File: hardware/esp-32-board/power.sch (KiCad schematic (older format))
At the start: 12 parts, among them J6 Barrel_Jack_MountingPin, SW3 SW_DPDT_x2, U4 NCP1117ST50T3G, U5 NCP1117-3.3

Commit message: Fix ERC errors in schematic
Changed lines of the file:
@@
 Wire Wire Line
 	5750 3300 5850 3300
-Text HLabel 5750 3300 0    50   UnSpc ~ 0
-Internal_3V3
 Text HLabel 6350 3400 2    50   UnSpc ~ 0
 +3.3V
@@
 Wire Wire Line
 	3400 3250 3950 3250
-Text HLabel 3950 3250 2    50   UnSpc ~ 0
-Internal_3V3
 Connection ~ 1950 3250
 Wire Wire Line
@@
 	2400 1550 2800 1550
 NoConn ~ 5850 3500
+Text Label 3950 3250 0    50   ~ 0
+Internal_3V3
+Text Label 5750 3300 2    50   ~ 0
+Internal_3V3
 $EndSCHEMATC

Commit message: Expose 5V instead of VIN on main connector
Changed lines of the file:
@@
 	1850 1550 2100 1550
 Wire Wire Line
-	2400 1550 2800 1550
+	2400 1550 2650 1550
 NoConn ~ 5850 3500
 Text Label 3950 3250 0    50   ~ 0
@@
 Text Label 5750 3300 2    50   ~ 0
 Internal_3V3
+$Comp
+L power:PWR_FLAG #FLG0101
+U 1 1 5FFE3888
+P 2650 1500
+F 0 "#FLG0101" H 2650 1575 50  0001 C CNN
+F 1 "PWR_FLAG" H 2650 1700 50  0000 C CNN
+F 2 "" H 2650 1500 50  0001 C CNN
+F 3 "~" H 2650 1500 50  0001 C CNN
+	1    2650 1500
+	1    0    0    -1
+$EndComp
+Wire Wire Line
+	2650 1550 2650 1500
+Connection ~ 2650 1550
+Wire Wire Line
+	2650 1550 2800 1550
 $EndSCHEMATC

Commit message: Replace power switch with jumper, add RX/TX leds
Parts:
- J7: renamed from SW3; value SW_DPDT_x2 -> Conn_01x02; footprint Button_Switch_SMD:Nidec_CL-SB-22B-0X -> Connector_PinHeader_2.54mm:PinHeader_1x02_P2.54mm_Vertical; symbol Switch:SW_DPDT_x2 -> Connector_Generic:Conn_01x02; Vendor tme.eu -> (none); VendorLink https://www.tme.eu/pl/details/cl-sb-22b-01/przelaczniki-suw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 -> (none)
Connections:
- no-connect marks 1 -> 0
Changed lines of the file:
@@
 VIN
 Wire Wire Line
-	6250 3400 6350 3400
+	5850 3500 5750 3500
 Wire Wire Line
-	5750 3300 5850 3300
-Text HLabel 6350 3400 2    50   UnSpc ~ 0
+	5750 3400 5850 3400
+Text HLabel 5750 3500 0    50   UnSpc ~ 0
 +3.3V
 $Comp
-L Switch:SW_DPDT_x2 SW3
+L Connector_Generic:Conn_01x02 J7
 U 1 1 5FE84590
 P 6050 3400
-F 0 "SW3" H 6050 3650 50  0000 C CNN
-F 1 "SW_DPDT_x2" H 6050 3550 50  0000 C CNN
-F 2 "Button_Switch_SMD:Nidec_CL-SB-22B-0X" H 6050 3050 50  0001 C CNN
-F 3 "https://www.tme.eu/Document/3439bdb81b005bcee4b59ba949df073a/seriaCL-SB.pdf" H 6050 3400 50  0001 C CNN
-F 4 "tme.eu" H 6050 3400 50  0001 C CNN "Vendor"
-F 5 "https://www.tme.eu/pl/details/cl-sb-22b-01/przelaczniki-suwakowe/nidec-copal-electronics/" H 6050 3400 50  0001 C CNN "VendorLink"
+F 0 "J7" H 6050 3650 50  0000 C CNN
+F 1 "Conn_01x02" H 6050 3550 50  0000 C CNN
+F 2 "Connector_PinHeader_2.54mm:PinHeader_1x02_P2.54mm_Vertical" H 6050 3050 50  0001 C CNN
+F 3 "~" H 6050 3400 50  0001 C CNN
+F 4 "" H 6050 3400 50  0001 C CNN "Vendor"
+F 5 "" H 6050 3400 50  0001 C CNN "VendorLink"
 	1    6050 3400
-	-1   0    0    -1
+	1    0    0    -1
 $EndComp
 Connection ~ 3400 3250
@@
 Text Notes 5200 2850 0    100  ~ 20
 Power switch for ESP-32
-Text Notes 5250 3950 0    50   ~ 0
+Text Notes 5250 4350 0    50   ~ 0
 Allows to disconnect ESP-32's 3.3V from regulators.\nUseful when board is powered externally by 3.3V port, preventing\ncurrent from "leaking" in unused USB and power circuit.
 $Comp
@@
 Wire Wire Line
 	2400 1550 2650 1550
-NoConn ~ 5850 3500
 Text Label 3950 3250 0    50   ~ 0
 Internal_3V3
-Text Label 5750 3300 2    50   ~ 0
+Text Label 5750 3400 2    50   ~ 0
 Internal_3V3
 $Comp

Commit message: Move LEDs
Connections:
- net +5V: now also D3.2 (A); no longer R4.1
- net GND: now also R4.2; no longer D3.1 (K)
- new net: D3.1 (K), R4.1
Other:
- moved on the sheet: D3, R4
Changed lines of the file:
@@
 L Device:R R?
 U 1 1 5FD3648C
-P 1950 3450
+P 1950 3800
 AR Path="/5FD3648C" Ref="R?"  Part="1"
 AR Path="/5FF6344B/5FD3648C" Ref="R4"  Part="1"
-F 0 "R4" H 1800 3550 50  0000 L CNN
-F 1 "220 Ohm" H 1650 3400 50  0000 L CNN
-F 2 "Resistor_SMD:R_0805_2012Metric_Pad1.20x1.40mm_HandSolder" V 1880 3450 50  0001 C CNN
-F 3 "~" H 1950 3450 50  0001 C CNN
-F 4 "avt.pl" H 1950 3450 50  0001 C CNN "Vendor"
-F 5 "https://sklep.avt.pl/avt701-805.html" H 1950 3450 50  0001 C CNN "VendorLink"
-	1    1950 3450
+F 0 "R4" H 1800 3900 50  0000 L CNN
+F 1 "220 Ohm" H 1650 3750 50  0000 L CNN
+F 2 "Resistor_SMD:R_0805_2012Metric_Pad1.20x1.40mm_HandSolder" V 1880 3800 50  0001 C CNN
+F 3 "~" H 1950 3800 50  0001 C CNN
+F 4 "avt.pl" H 1950 3800 50  0001 C CNN "Vendor"
+F 5 "https://sklep.avt.pl/avt701-805.html" H 1950 3800 50  0001 C CNN "VendorLink"
+	1    1950 3800
 	1    0    0    -1
 $EndComp
@@
 L Device:LED D?
 U 1 1 5FD36465
-P 1950 3800
+P 1950 3450
 AR Path="/5FD36465" Ref="D?"  Part="1"
 AR Path="/5FF6344B/5FD36465" Ref="D3"  Part="1"
-F 0 "D3" V 1950 3950 50  0000 C CNN
-F 1 "RF-GSS150TS-BC" V 2050 3950 50  0000 C CNN
-F 2 "LED_SMD:LED_1206_3216Metric_Pad1.42x1.75mm_HandSolder" H 1950 3800 50  0001 C CNN
-F 3 "https://www.tme.eu/Document/297bac1c849d293b517ecf72110c4a89/catalouge-REFOND.pdf" H 1950 3800 50  0001 C CNN
-F 4 "tme.eu" H 1950 3800 50  0001 C CNN "Vendor"
-F 5 "https://www.tme.eu/pl/details/rf-gss150ts-bc/diody-led-smd-kolorowe/refond/" H 1950 3800 50  0001 C CNN "VendorLink"
-	1    1950 3800
+F 0 "D3" V 1950 3600 50  0000 C CNN
+F 1 "RF-GSS150TS-BC" V 2050 3600 50  0000 C CNN
+F 2 "LED_SMD:LED_1206_3216Metric_Pad1.42x1.75mm_HandSolder" H 1950 3450 50  0001 C CNN
+F 3 "https://www.tme.eu/Document/297bac1c849d293b517ecf72110c4a89/catalouge-REFOND.pdf" H 1950 3450 50  0001 C CNN
+F 4 "tme.eu" H 1950 3450 50  0001 C CNN "Vendor"
+F 5 "https://www.tme.eu/pl/details/rf-gss150ts-bc/diody-led-smd-kolorowe/refond/" H 1950 3450 50  0001 C CNN "VendorLink"
+	1    1950 3450
 	0    -1   -1   0
 $EndComp

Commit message: Reannotate schematic
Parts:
- renumbered C8 to C5, C9 to C6, C5 to C7, C6 to C8, C7 to C9, D3 to D1, J6 to J5, J7 to J6, R4 to R1, U5 to U2, U4 to U3
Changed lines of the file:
@@
 P 1550 1650
 AR Path="/5FB78030" Ref="J?"  Part="1"
-AR Path="/5FF6344B/5FB78030" Ref="J6"  Part="1"
-F 0 "J6" H 1300 1400 50  0000 C CNN
+AR Path="/5FF6344B/5FB78030" Ref="J5"  Part="1"
+F 0 "J5" H 1300 1400 50  0000 C CNN
 F 1 "Barrel_Jack_MountingPin" H 1500 1900 50  0000 C CNN
 F 2 "Connector_BarrelJack:BarrelJack_Lumberg_1613-21_Horizontal" H 1600 1610 50  0001 C CNN
@@
 P 6300 1550
 AR Path="/5FB78036" Ref="U?"  Part="1"
-AR Path="/5FF6344B/5FB78036" Ref="U4"  Part="1"
-F 0 "U4" H 6300 1850 50  0000 C CNN
+AR Path="/5FF6344B/5FB78036" Ref="U3"  Part="1"
+F 0 "U3" H 6300 1850 50  0000 C CNN
 F 1 "NCP1117ST50T3G" H 6300 1750 50  0000 C CNN
 F 2 "Package_TO_SOT_SMD:SOT-223-3_TabPin2" H 6300 1775 50  0001 C CIN
@@
 P 5900 1800
 AR Path="/5FB78047" Ref="C?"  Part="1"
-AR Path="/5FF6344B/5FB78047" Ref="C5"  Part="1"
-F 0 "C5" H 5650 1900 50  0000 L CNN
+AR Path="/5FF6344B/5FB78047" Ref="C7"  Part="1"
+F 0 "C7" H 5650 1900 50  0000 L CNN
 F 1 "47uF" H 5600 1750 50  0000 L CNN
 F 2 "Capacitor_SMD:CP_Elec_5x5.9" H 5938 1650 50  0001 C CNN
@@
 P 6700 1800
 AR Path="/5FB7804D" Ref="C?"  Part="1"
-AR Path="/5FF6344B/5FB7804D" Ref="C6"  Part="1"
-F 0 "C6" H 6800 1900 50  0000 L CNN
+AR Path="/5FF6344B/5FB7804D" Ref="C8"  Part="1"
+F 0 "C8" H 6800 1900 50  0000 L CNN
 F 1 "47uF" H 6800 1750 50  0000 L CNN
 F 2 "Capacitor_SMD:CP_Elec_5x5.9" H 6738 1650 50  0001 C CNN
@@
 P 7200 1800
 AR Path="/5FB78060" Ref="C?"  Part="1"
-AR Path="/5FF6344B/5FB78060" Ref="C7"  Part="1"
-F 0 "C7" H 7300 1900 50  0000 L CNN
+AR Path="/5FF6344B/5FB78060" Ref="C9"  Part="1"
+F 0 "C9" H 7300 1900 50  0000 L CNN
 F 1 "100nF" H 7300 1750 50  0000 L CNN
 F 2 "Capacitor_SMD:C_0805_2012Metric_Pad1.18x1.45mm_HandSolder" H 7238 1650 50  0001 C CNN
@@
 +3.3V
 $Comp
-L Connector_Generic:Conn_01x02 J7
+L Connector_Generic:Conn_01x02 J6
 U 1 1 5FE84590
 P 6050 3400
-F 0 "J7" H 6050 3650 50  0000 C CNN
+F 0 "J6" H 6050 3650 50  0000 C CNN
 F 1 "Conn_01x02" H 6050 3550 50  0000 C CNN
 F 2 "Connector_PinHeader_2.54mm:PinHeader_1x02_P2.54mm_Vertical" H 6050 3050 50  0001 C CNN
@@
 P 1950 3800
 AR Path="/5FD3648C" Ref="R?"  Part="1"
-AR Path="/5FF6344B/5FD3648C" Ref="R4"  Part="1"
-F 0 "R4" H 1800 3900 50  0000 L CNN
+AR Path="/5FF6344B/5FD3648C" Ref="R1"  Part="1"
+F 0 "R1" H 1800 3900 50  0000 L CNN
 F 1 "220 Ohm" H 1650 3750 50  0000 L CNN
 F 2 "Resistor_SMD:R_0805_2012Metric_Pad1.20x1.40mm_HandSolder" V 1880 3800 50  0001 C CNN
@@
 P 2300 3600
 AR Path="/5FD36471" Ref="C?"  Part="1"
-AR Path="/5FF6344B/5FD36471" Ref="C8"  Part="1"
-F 0 "C8" H 2350 3700 50  0000 L CNN
+AR Path="/5FF6344B/5FD36471" Ref="C5"  Part="1"
+F 0 "C5" H 2350 3700 50  0000 L CNN
 F 1 "22uF" H 2350 3500 50  0000 L CNN
 F 2 "Capacitor_SMD:C_0805_2012Metric_Pad1.18x1.45mm_HandSolder" H 2338 3450 50  0001 C CNN
@@
 P 3400 3600
 AR Path="/5FD3646B" Ref="C?"  Part="1"
-AR Path="/5FF6344B/5FD3646B" Ref="C9"  Part="1"
-F 0 "C9" H 3500 3700 50  0000 L CNN
+AR Path="/5FF6344B/5FD3646B" Ref="C6"  Part="1"
+F 0 "C6" H 3500 3700 50  0000 L CNN
 F 1 "22uF" H 3500 3500 50  0000 L CNN
 F 2 "Capacitor_SMD:C_0805_2012Metric_Pad1.18x1.45mm_HandSolder" H 3438 3450 50  0001 C CNN
@@
 P 1950 3450
 AR Path="/5FD36465" Ref="D?"  Part="1"
-AR Path="/5FF6344B/5FD36465" Ref="D3"  Part="1"
-F 0 "D3" V 1950 3600 50  0000 C CNN
+AR Path="/5FF6344B/5FD36465" Ref="D1"  Part="1"
+F 0 "D1" V 1950 3600 50  0000 C CNN
 F 1 "RF-GSS150TS-BC" V 2050 3600 50  0000 C CNN
 F 2 "LED_SMD:LED_1206_3216Metric_Pad1.42x1.75mm_HandSolder" H 1950 3450 50  0001 C CNN
@@
 P 2700 3250
 AR Path="/5FD3645F" Ref="U?"  Part="1"
-AR Path="/5FF6344B/5FD3645F" Ref="U5"  Part="1"
-F 0 "U5" H 2700 3550 50  0000 C CNN
+AR Path="/5FF6344B/5FD3645F" Ref="U2"  Part="1"
+F 0 "U2" H 2700 3550 50  0000 C CNN
 F 1 "NCP1117-3.3" H 2700 3450 50  0000 C CNN
 F 2 "Package_TO_SOT_SMD:SOT-223-3_TabPin2" H 2700 3450 50  0001 C CNN
@@
 Internal_3V3
 $Comp
-L power:PWR_FLAG #FLG0101
+L power:PWR_FLAG #FLG02
 U 1 1 5FFE3888
 P 2650 1500
-F 0 "#FLG0101" H 2650 1575 50  0001 C CNN
+F 0 "#FLG02" H 2650 1575 50  0001 C CNN
 F 1 "PWR_FLAG" H 2650 1700 50  0000 C CNN
 F 2 "" H 2650 1500 50  0001 C CNN

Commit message: Replace Micro USB and button components (no products in stock)
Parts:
- C9: value 100nF -> 0.1uF
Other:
- note removed: "Internal 3.3V powers\nUSB-UART converter"
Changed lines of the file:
@@
 AR Path="/5FF6344B/5FB78060" Ref="C9"  Part="1"
 F 0 "C9" H 7300 1900 50  0000 L CNN
-F 1 "100nF" H 7300 1750 50  0000 L CNN
+F 1 "0.1uF" H 7300 1750 50  0000 L CNN
 F 2 "Capacitor_SMD:C_0805_2012Metric_Pad1.18x1.45mm_HandSolder" H 7238 1650 50  0001 C CNN
 F 3 "~" H 7200 1800 50  0001 C CNN
@@
 Text Notes 900  3650 0    50   ~ 0
 5V may come\nfrom DC-5V\nregulator or\nfrom USB
-Text Notes 3850 3500 0    50   ~ 0
-Internal 3.3V powers\nUSB-UART converter
 Text Notes 5200 2850 0    100  ~ 20
 Power switch for ESP-32

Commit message: Change DC connector to CLIFF FC68148
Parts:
- J5: footprint Connector_BarrelJack:BarrelJack_Lumberg_1613-21_Horizontal -> Connector_BarrelJack:BarrelJack_CLIFF_FC68148_Horizontal
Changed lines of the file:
@@
 F 0 "J5" H 1300 1400 50  0000 C CNN
 F 1 "Barrel_Jack_MountingPin" H 1500 1900 50  0000 C CNN
-F 2 "Connector_BarrelJack:BarrelJack_Lumberg_1613-21_Horizontal" H 1600 1610 50  0001 C CNN
+F 2 "Connector_BarrelJack:BarrelJack_CLIFF_FC68148_Horizontal" H 1600 1610 50  0001 C CNN
 F 3 "https://www.tme.eu/Document/3d585bc2823a1d150d9d924b483e2fef/1613-21.pdf" H 1600 1610 50  0001 C CNN
 F 4 "tme.eu" H 1550 1650 50  0001 C CNN "Vendor"

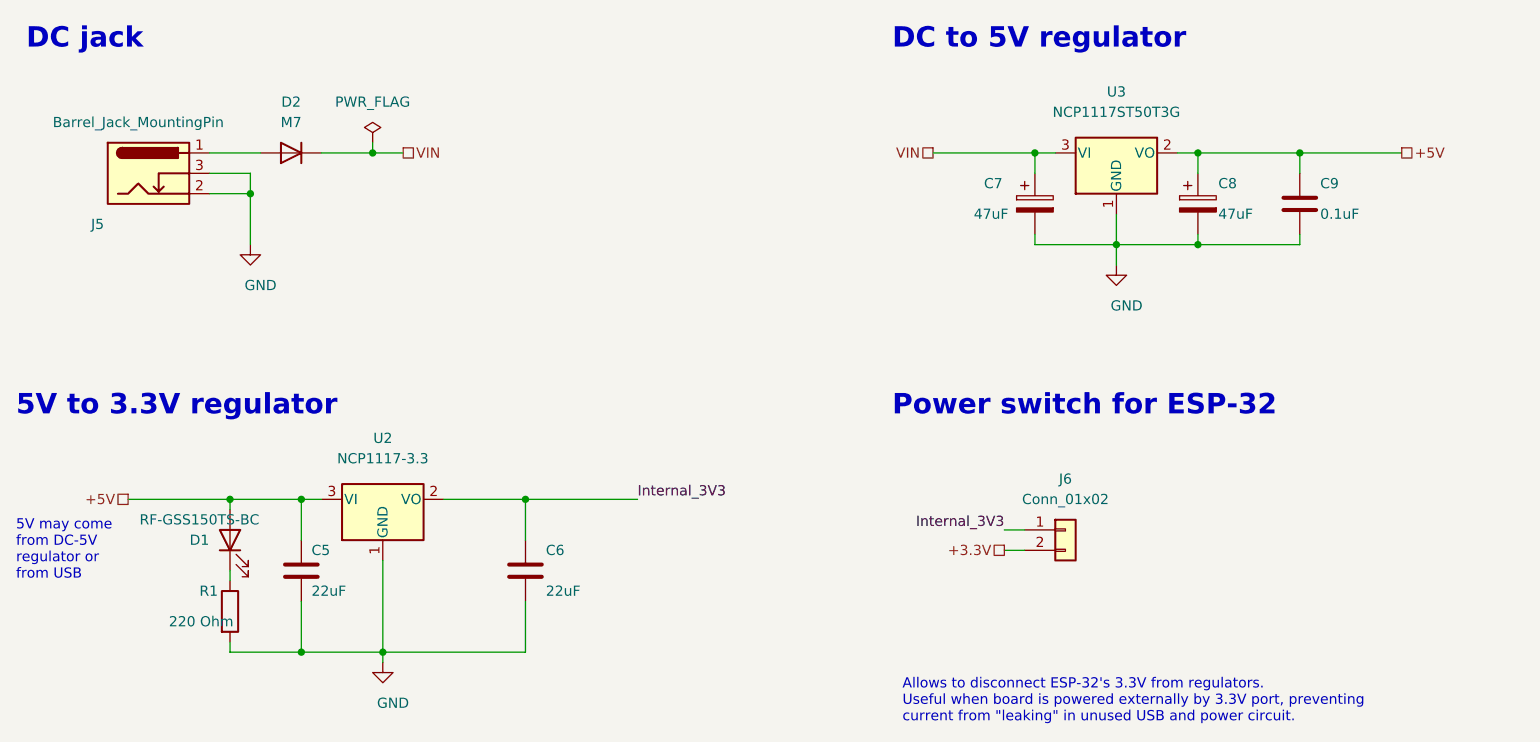
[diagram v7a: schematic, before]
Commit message: Remove power switch
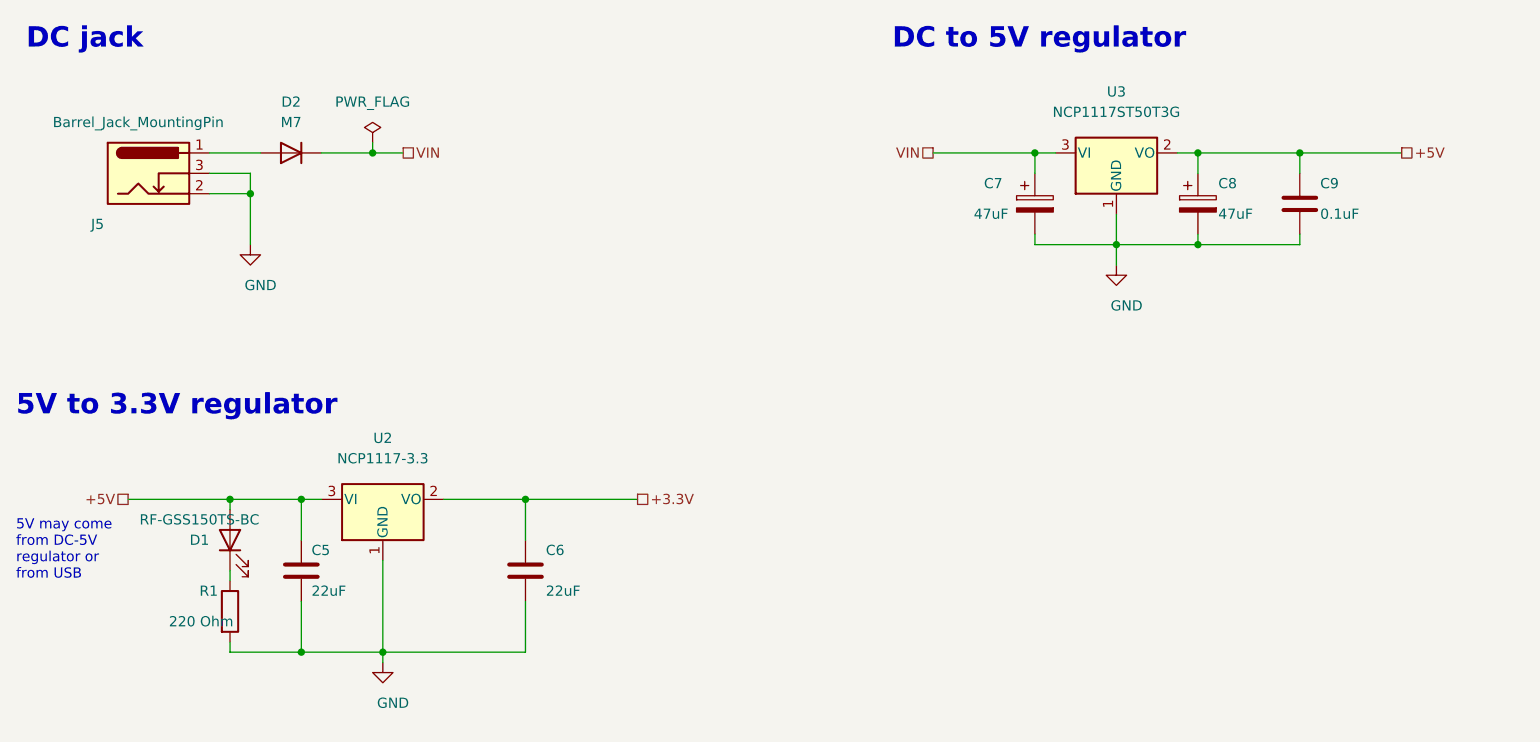
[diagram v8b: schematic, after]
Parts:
- removed J6: Conn_01x02, Connector_PinHeader_2.54mm:PinHeader_1x02_P2.54mm_Vertical, symbol Connector_Generic:Conn_01x02
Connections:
- net Internal_3V3 is gone; now on net +3.3V: C6.1, U2.2 (VO)
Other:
- note removed: "Allows to disconnect ESP-32's 3.3V from regulators.\nUseful when board is powered externally by 3.3V port, preventing\ncurrent from "leaking" in unused USB and power circuit."
- note removed: "Power switch for ESP-32"
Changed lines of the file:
@@
 Text HLabel 5400 1550 0    50   UnSpc ~ 0
 VIN
-Wire Wire Line
-	5850 3500 5750 3500
-Wire Wire Line
-	5750 3400 5850 3400
-Text HLabel 5750 3500 0    50   UnSpc ~ 0
+Text HLabel 3950 3250 2    50   UnSpc ~ 0
 +3.3V
-$Comp
-L Connector_Generic:Conn_01x02 J6
-U 1 1 5FE84590
-P 6050 3400
-F 0 "J6" H 6050 3650 50  0000 C CNN
-F 1 "Conn_01x02" H 6050 3550 50  0000 C CNN
-F 2 "Connector_PinHeader_2.54mm:PinHeader_1x02_P2.54mm_Vertical" H 6050 3050 50  0001 C CNN
-F 3 "~" H 6050 3400 50  0001 C CNN
-F 4 "" H 6050 3400 50  0001 C CNN "Vendor"
-F 5 "" H 6050 3400 50  0001 C CNN "VendorLink"
-	1    6050 3400
-	1    0    0    -1
-$EndComp
 Connection ~ 3400 3250
 Wire Wire Line
@@
 Text Notes 900  3650 0    50   ~ 0
 5V may come\nfrom DC-5V\nregulator or\nfrom USB
-Text Notes 5200 2850 0    100  ~ 20
-Power switch for ESP-32
-Text Notes 5250 4350 0    50   ~ 0
-Allows to disconnect ESP-32's 3.3V from regulators.\nUseful when board is powered externally by 3.3V port, preventing\ncurrent from "leaking" in unused USB and power circuit.
 $Comp
 L Regulator_Linear:NCP1117-3.3_SOT223 U?
@@
 Wire Wire Line
 	2400 1550 2650 1550
-Text Label 3950 3250 0    50   ~ 0
-Internal_3V3
-Text Label 5750 3400 2    50   ~ 0
-Internal_3V3
 $Comp
 L power:PWR_FLAG #FLG02
